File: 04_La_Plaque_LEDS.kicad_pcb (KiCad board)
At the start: 2 copper layers, 100 x 100 mm, 133 parts, among them J1 Conn_01x04

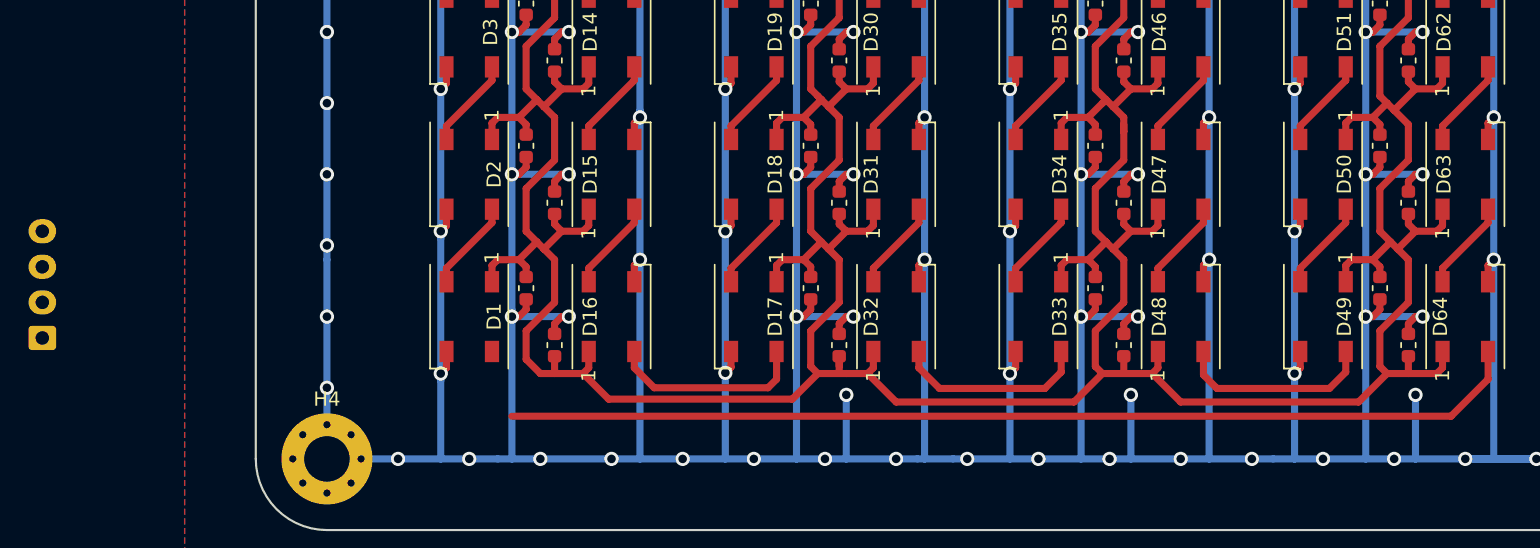
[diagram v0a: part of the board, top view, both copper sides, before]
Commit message: jst coudé
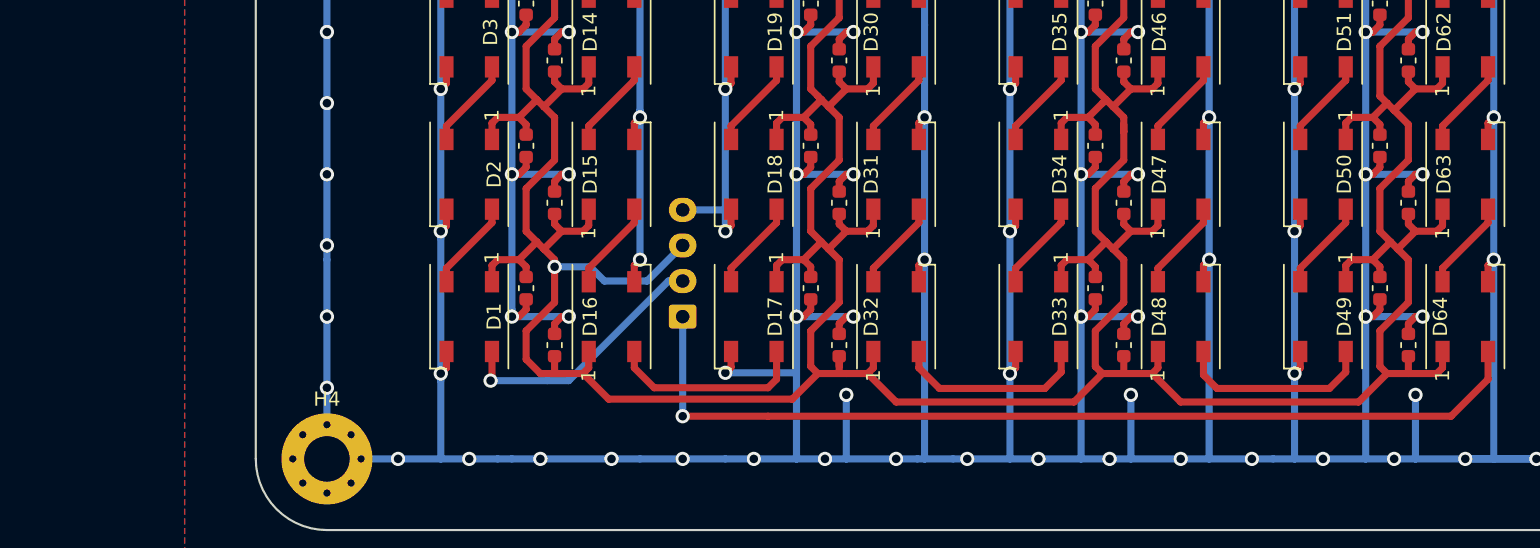
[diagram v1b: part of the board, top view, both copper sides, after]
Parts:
- J1: footprint Connector_JST:JST_XH_B4B-XH-A_1x04_P2.50mm_Vertical -> Connector_JST:JST_XH_S4B-XH-A_1x04_P2.50mm_Horizontal
- moved J1 45.0 mm to (130.0, 140.0)
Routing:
- net GND: track 1823.7 -> 1791.7 mm
- net S0: track 0.00 -> 18.5 mm, vias 0 -> 1
- net +5V: track 828.9 -> 839.3 mm, vias 0 -> 1
- net back0: track 71.6 -> 66.6 mm, vias 0 -> 1

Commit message: tourné connecteur + silks
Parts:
- moved J1 7.50 mm to (130.0, 132.5), turned to 270 degrees
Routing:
- net back0: track 66.6 -> 75.7 mm
- net S0: track 18.5 -> 25.4 mm, vias 1 -> 2
- net GND: track 1791.7 -> 1796.7 mm
- net +5V: track 839.3 -> 838.3 mm
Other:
- board text added: "GND +5V S0 back0"
- board text added: "La_plaque_LEDS 2020/12/06"
- board text removed: "+5V GND S0 back0"
- board text removed: "TOR_plaque_leds 8/11/2020"
